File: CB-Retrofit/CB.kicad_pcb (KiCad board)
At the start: 2 copper layers, 180 x 56 mm, 21 parts, among them SW1 SW_SPST, SW2 3pdt, SW3 SW_Push, U1 PBOOST500, U2 SD_Card_Module, U3 Teensy3.2, U4 AUDIOB_I2S, U5 TDA1543, U6 LM386

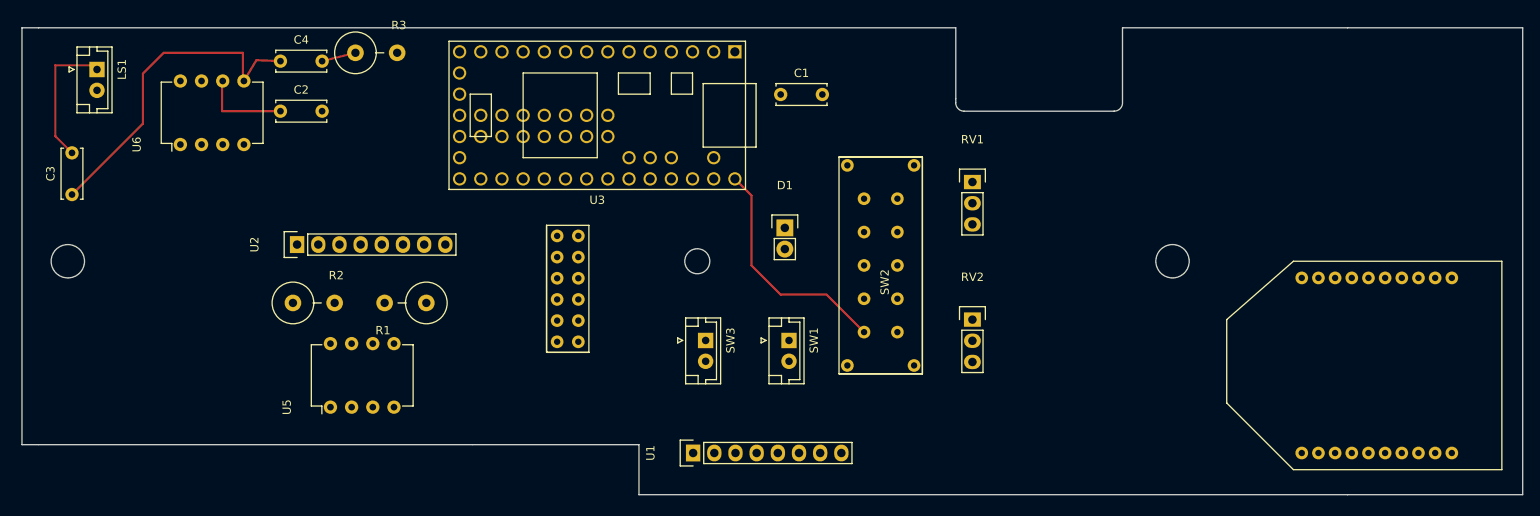
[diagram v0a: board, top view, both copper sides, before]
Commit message: First possible PCB, needs a few more footprints
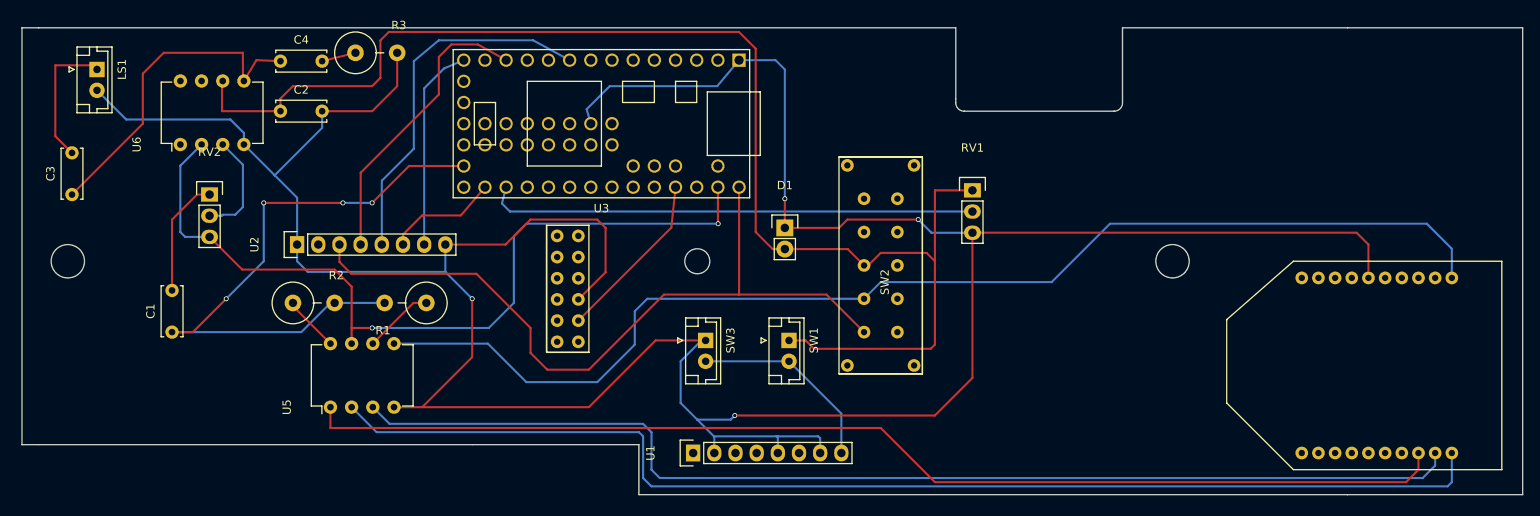
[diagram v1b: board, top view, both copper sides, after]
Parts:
- moved RV2 92.7 mm to (95.5, 80.0)
- moved C1 78.4 mm to (91.0, 96.5), turned to 90 degrees
- moved U3 1.12 mm to (142.5, 71.5)
- moved RV1 1.00 mm to (187.0, 79.5)
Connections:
- S1 pad 11: Net-(S1-Pad11) -> /PTT
- SW2 pad 8: GND -> Net-(SW2-Pad8)
- U2 pad 3: +5V -> /TEENSY_POW
- U3 pad 30: Net-(U3-Pad30) -> /PTT
- U3 pad 4: Net-(S1-Pad11) -> Net-(U3-Pad4)
- U3 pad 5: Net-(SW2-Pad6) -> Net-(U3-Pad5)
- U3 pad 6: Net-(SW2-Pad7) -> Net-(U3-Pad6)
- U3 pad 7: Net-(SW2-Pad9) -> Net-(U3-Pad7)
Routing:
- net GND: track 0.00 -> 384.4 mm, vias 0 -> 4
- net +5V: track 10.7 -> 163.2 mm
- net /BT_POW: track 0.00 -> 143.7 mm
- net Net-(U4-Pad10): track 0.00 -> 142.5 mm
- net Net-(U4-Pad8): track 0.00 -> 138.3 mm
- net Net-(U4-Pad9): track 0.00 -> 135.7 mm
- net GNDA: track 0.00 -> 99.9 mm, vias 0 -> 2
- net /LINE_OUT: track 0.00 -> 74.3 mm, vias 0 -> 4
- net /TEENSY_POW: track 28.0 -> 90.6 mm
- net Net-(RV1-Pad2): track 0.00 -> 58.8 mm
- net /DO: track 0.00 -> 43.8 mm
- net /CS: track 0.00 -> 35.6 mm
- net /DI: track 0.00 -> 24.7 mm
- net Net-(SW1-Pad2): track 0.00 -> 23.6 mm
- net /PTT: track 0.00 -> 20.6 mm
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
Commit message: Second attempt
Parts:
- added J1: PowerJack, 4pdt:Power_Jack, F.Cu at (211.5, 64.0)
- added J2: POT_MOUNT, 4pdt:POT_MOUNT, F.Cu at (201.5, 92.5)
- added SW4: SW_Push, Connectors_JST:JST_EH_B02B-EH-A_02x2.50mm_Straight, F.Cu at (241.5, 83.0)
- SW2: value 3pdt -> SW_SPST; footprint 4pdt:3pdt -> Connectors_JST:JST_EH_B02B-EH-A_02x2.50mm_Straight
- SW3: value SW_Push -> 3pdt; footprint Connectors_JST:JST_EH_B02B-EH-A_02x2.50mm_Straight -> 4pdt:3pdt
- moved RV1 102.7 mm to (85.0, 91.5)
- moved U1 71.0 mm to (224.5, 109.5)
- moved D1 57.5 mm to (222.0, 85.5), turned to 180 degrees
- moved SW2 55.5 mm to (231.0, 83.0), turned to 0 degrees
- moved U5 44.5 mm to (154.0, 112.0)
- moved R2 44.2 mm to (152.0, 97.0)
- moved R1 42.2 mm to (161.0, 97.0)
- moved U4 40.2 mm to (196.0, 92.5), turned to 0 degrees
- moved C1 39.3 mm to (129.5, 104.5), turned to 180 degrees
- moved RV2 36.9 mm to (131.0, 90.0)
- moved SW1 34.3 mm to (176.0, 65.0), turned to 0 degrees
- moved U2 33.4 mm to (78.5, 105.0)
- moved C2 27.5 mm to (77.0, 75.0), turned to 270 degrees
- moved SW3 23.2 mm to (177.0, 90.0), turned to 90 degrees
- moved C3 15.3 mm to (87.0, 67.0), turned to 180 degrees
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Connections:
- SW1 pad 1: +5V -> Net-(SW1-Pad1)
- SW2 pad 1: /TEENSY_POW -> +5V
- SW2 pad 2: /BT_POW -> Net-(SW2-Pad2)
- SW3 pad 1: GND -> /TEENSY_POW
- SW3 pad 2: Net-(SW1-Pad2) -> /BT_POW
- U1 pad 8: Net-(SW1-Pad2) -> Net-(SW2-Pad2)
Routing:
- net GND: track 384.4 -> 0.00 mm, vias 4 -> 0
- net Net-(U4-Pad10): track 142.5 -> 34.0 mm
- net Net-(U4-Pad8): track 138.3 -> 37.0 mm
- net Net-(U4-Pad9): track 135.7 -> 48.2 mm
- net /BT_POW: track 143.7 -> 59.1 mm
- net VCC: track 0.00 -> 83.7 mm
- net Net-(RV1-Pad2): track 58.8 -> 0.00 mm
- net Net-(RV2-Pad2): track 12.9 -> 61.0 mm
- net Net-(SW2-Pad2): track 0.00 -> 46.2 mm
- net /DO: track 43.8 -> 0.00 mm
- net /CS: track 35.6 -> 0.00 mm
- net /PTT: track 20.6 -> 49.8 mm
- net /DI: track 24.7 -> 0.00 mm
- net Net-(SW1-Pad2): track 23.6 -> 0.00 mm
- net Net-(C3-Pad1): track 40.5 -> 17.2 mm
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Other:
- board text added: "PTT"
